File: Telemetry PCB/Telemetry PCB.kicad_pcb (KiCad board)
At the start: 2 copper layers, 56.8 x 42.2 mm, 53 parts, among them J1 Conn_01x02_Male, J2 Conn_01x05_Male, J3 Conn_01x04_Male, J4 Conn_01x02_Male, J5 Conn_01x02_Male, J6 CON-SMA-EDGE-S, U1 ADF7023-JBCPZ, U2 LP2985-3.3, U3 0900PC15F0030, Y1 NX1612AA-26MHZ-TI2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

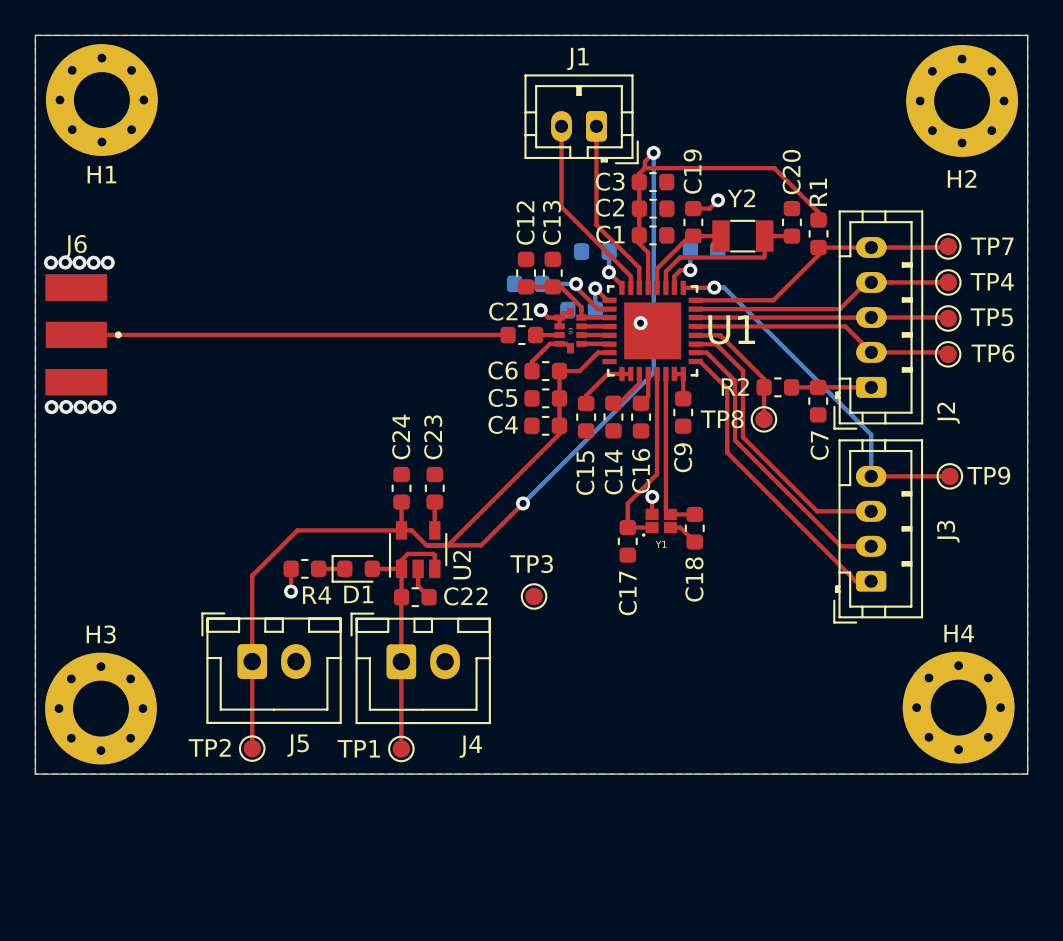
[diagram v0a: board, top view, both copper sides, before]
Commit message: Telemetry PCB: Fixed various clearance issues and improved layout.
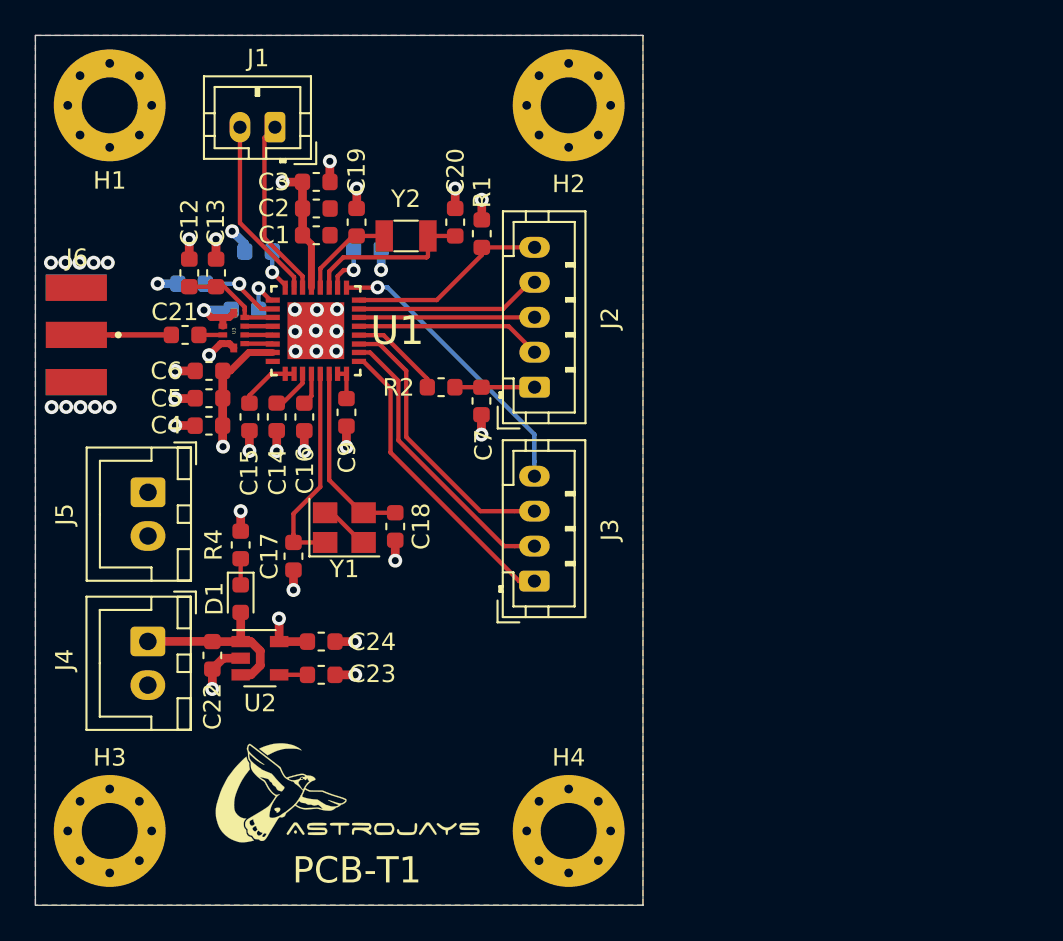
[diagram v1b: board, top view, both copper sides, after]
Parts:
- removed TP1: TP_5V, TestPoint:TestPoint_Pad_D1.0mm
- removed TP2: TP_3V3, TestPoint:TestPoint_Pad_D1.0mm
- removed TP3: TP_GND, TestPoint:TestPoint_Pad_D1.0mm
- removed TP4: TP_MOSI, TestPoint:TestPoint_Pad_D1.0mm
- removed TP5: TP_CLK, TestPoint:TestPoint_Pad_D1.0mm
- removed TP6: TP_MISO, TestPoint:TestPoint_Pad_D1.0mm
- removed TP7: TP_CS, TestPoint:TestPoint_Pad_D1.0mm
- removed TP8: TP_IRQ, TestPoint:TestPoint_Pad_D1.0mm
- removed TP9: TP_GP4, TestPoint:TestPoint_Pad_D1.0mm
- added G***: LOGO, AJ_GFX:full_logo_21.3mmx9.3mm, F.Cu at (127.0, 123.0)
- Y1: value NX1612AA-26MHZ-TI2 -> 26M; footprint Parts:OSCSC105P160X120X35-4N -> Crystal:Crystal_SMD_3225-4Pin_3.2x2.5mm
- moved H4 23.4 mm to (138.0, 125.5)
- moved H2 22.5 mm to (138.0, 84.0)
- moved C13 19.3 mm to (117.8, 93.6)
- moved C20 19.3 mm to (131.5, 90.7)
- moved C7 19.3 mm to (133.0, 100.9)
- moved J3 19.3 mm to (136.0, 111.2)
- moved R2 19.3 mm to (130.7, 100.1)
- moved Y2 19.3 mm to (128.7, 91.5)
- moved C10 19.3 mm to (126.5, 92.2)
- moved C11 19.3 mm to (119.5, 95.7)
- moved C12 19.3 mm to (116.3, 93.6)
- moved C14 19.3 mm to (121.3, 101.8)
- moved C15 19.3 mm to (119.7, 101.8)
- moved C4 19.3 mm to (117.4, 102.3)
- moved C5 19.3 mm to (117.4, 100.8)
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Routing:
- net +3V3: track 89.8 -> 19.1 mm, vias 2 -> 4
- net GND: track 14.2 -> 37.2 mm, vias 15 -> 43
- net Net-(C21-Pad2): track 24.7 -> 5.45 mm
- net +5V: track 15.3 -> 10.5 mm
- net /GP4: track 21.1 -> 16.6 mm
- net /MISO: track 15.1 -> 10.7 mm
- net /~CS: track 16.0 -> 11.6 mm
- net /SCLK: track 14.5 -> 10.0 mm
- net /MOSI: track 15.1 -> 10.7 mm
- net /IRQ: track 7.25 -> 5.42 mm
- net Net-(C17-Pad1): track 10.9 -> 12.1 mm
- net Net-(C18-Pad1): track 9.53 -> 10.6 mm
- added copper zone on In2.Cu, net +3V3
- added copper zone on In1.Cu, net GND
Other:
- board size 56.8 x 42.2 mm -> 34.8 x 49.8 mm
- copper layers 2 -> 4
- net class Default: clearance 0.1 -> 0.127
- net class Power added: clearance 0.127, trace_width 0.5, via_dia 0.8, via_drill 0.4
- net class RF added: clearance 0.127, trace_width 0.313741, via_dia 0.8, via_drill 0.4
- rule trace_clearance: 0.1 -> 0.127
- board text added: "PCB-T1"
- board text added: "Telemetry PCB - Rev 1.0 Part ID: PCB-T1 AstroJays Rocketry JHU, Jan 2022"
